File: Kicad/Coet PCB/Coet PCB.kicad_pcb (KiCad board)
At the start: 2 copper layers, 5 parts, among them U1 BNO055 Stemma, U2 Teensy4.1, U3 BMP280 Stemma, U4 MP1584EN, U5 XL4015_DC

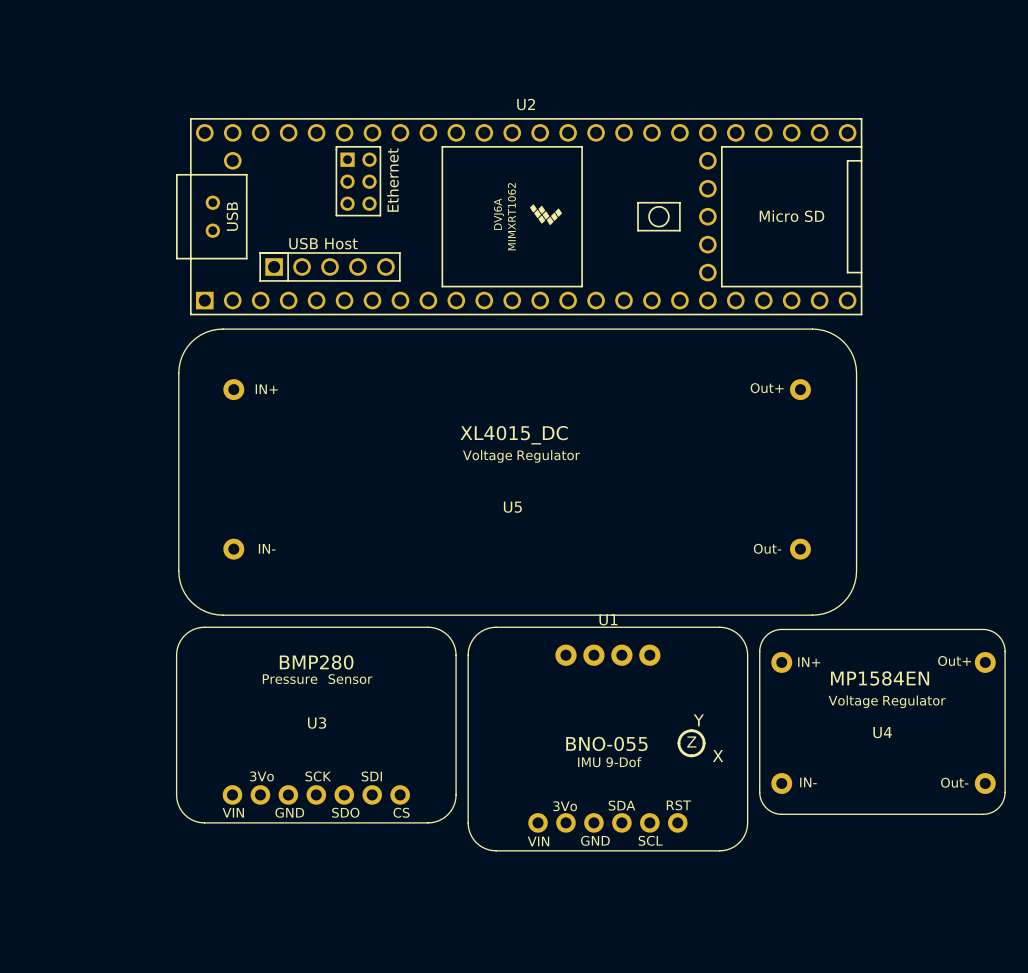
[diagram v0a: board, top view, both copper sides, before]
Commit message: Added the next libraries to Kicad: Teensy4.1, Bno055, Bmp280, MP1584EN, XL4015DC
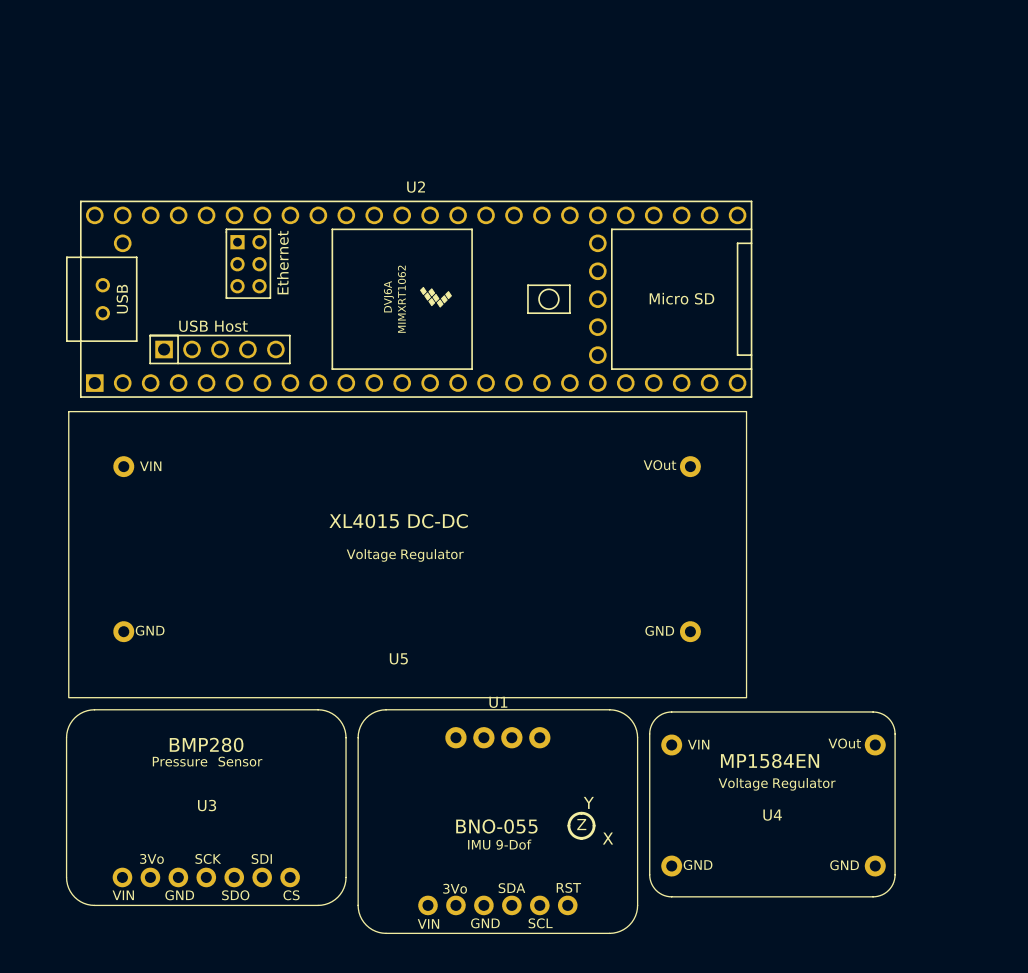
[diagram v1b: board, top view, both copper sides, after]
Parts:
- U5: footprint XL4015_DC:XL4015 -> XL4015DC:XL4015 DC-DC
- moved U5 12.5 mm to (90.2, 69.7)
- moved U1 12.5 mm to (129.3, 107.6)
- moved U3 12.5 mm to (102.8, 106.0)
- moved U4 12.5 mm to (154.1, 97.0)
- moved U2 12.5 mm to (121.8, 59.5)

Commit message: He acabat les conecions del esquema!
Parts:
- added BZ1: Buzzer, Buzzer_Beeper:Buzzer_TDK_PS1240P02BT_D12.2mm_H6.5mm, F.Cu at (130.0, 110.5)
- added C1_100uf1: C_US, Capacitor_SMD:CP_Elec_8x5.4, F.Cu at (154.5, 59.9)
- added C1_470uf1: C_US, Capacitor_SMD:CP_Elec_8x5.4, F.Cu at (154.5, 69.7)
- added D1: LED_ABGR, LED_THT:LED_D5.0mm-4_RGB_Wide_Pins, F.Cu at (150.0, 78.4)
- added M1: TVC1, Connector_PinHeader_1.00mm:PinHeader_1x03_P1.00mm_Vertical, F.Cu at (87.8, 84.5)
- added M2: TVC2, Connector_PinHeader_1.00mm:PinHeader_1x03_P1.00mm_Vertical, F.Cu at (87.8, 94.2)
- added M3: Parachute, Connector_PinHeader_1.00mm:PinHeader_1x03_P1.00mm_Vertical, F.Cu at (87.8, 103.9)
- added R1: R1, Resistor_THT:R_Axial_DIN0207_L6.3mm_D2.5mm_P10.16mm_Horizontal, F.Cu at (140.9, 105.7)
- added R2: R20, Resistor_THT:R_Axial_DIN0207_L6.3mm_D2.5mm_P10.16mm_Horizontal, F.Cu at (140.9, 109.7)
- added R3: R67, Resistor_THT:R_Axial_DIN0207_L6.3mm_D2.5mm_P10.16mm_Horizontal, F.Cu at (140.9, 113.8)
- moved U4 43.9 mm to (110.4, 101.9)
- moved U1 16.8 mm to (138.7, 93.6)
- moved U3 16.8 mm to (112.2, 92.0)
- moved U5 14.6 mm to (86.2, 55.7)
- moved U2 14.6 mm to (117.8, 45.5)
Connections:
- U1 pad 1: unconnected-(U1-Vin-Pad1) -> Net-(U1-Vin)
- U1 pad 3: unconnected-(U1-GND-Pad3) -> Net-(U1-GND)
- U1 pad 4: unconnected-(U1-SCL-Pad4) -> Net-(U1-SCL)
- U1 pad 5: unconnected-(U1-SDA-Pad5) -> Net-(U1-SDA)
- U2 pad 1: unconnected-(U2-GND-Pad1) -> Net-(BZ1--)
- U2 pad 10: unconnected-(U2-8_TX2_IN1-Pad10) -> Net-(U2-8_TX2_IN1)
- U2 pad 11: unconnected-(U2-9_OUT1C-Pad11) -> Net-(U2-9_OUT1C)
- U2 pad 12: unconnected-(U2-10_CS_MQSR-Pad12) -> Net-(U2-10_CS_MQSR)
- U2 pad 4: unconnected-(U2-2_OUT2-Pad4) -> Net-(BZ1-+)
- U2 pad 40: unconnected-(U2-18_A4_SDA-Pad40) -> Net-(U1-SDA)
- U2 pad 41: unconnected-(U2-19_A5_SCL-Pad41) -> Net-(U1-SCL)
- U2 pad 47: unconnected-(U2-GND-Pad47) -> Net-(U1-GND)
- U2 pad 48: unconnected-(U2-VIN-Pad48) -> Net-(U1-Vin)
- U4 pad 1: unconnected-(U4-IN+-Pad1) -> +BATT
- U4 pad 2: unconnected-(U4-IN--Pad2) -> GND
- U4 pad 3: unconnected-(U4-Out+-Pad3) -> Net-(U4-VOut)
- U4 pad 4: unconnected-(U4-Out--Pad4) -> Net-(BZ1--)
- U5 pad 1: unconnected-(U5-VIN-Pad1) -> +BATT
- U5 pad 2: unconnected-(U5-GND-Pad2) -> GND
- U5 pad 3: unconnected-(U5-VOut-Pad3) -> Net-(U5-VOut)
- U5 pad 4: unconnected-(U5-GND-Pad4) -> Net-(BZ1--)
